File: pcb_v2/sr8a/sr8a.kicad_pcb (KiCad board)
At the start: 2 copper layers, 125.7 x 55.2 mm, 23 parts, among them J2 conn, U1 74LS574, U10 74LS00, U2 74LS574, U3 74LS574, U4 74LS574, U5 74LS574, U6 74LS574, U7 74LS574, U8 74HC238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

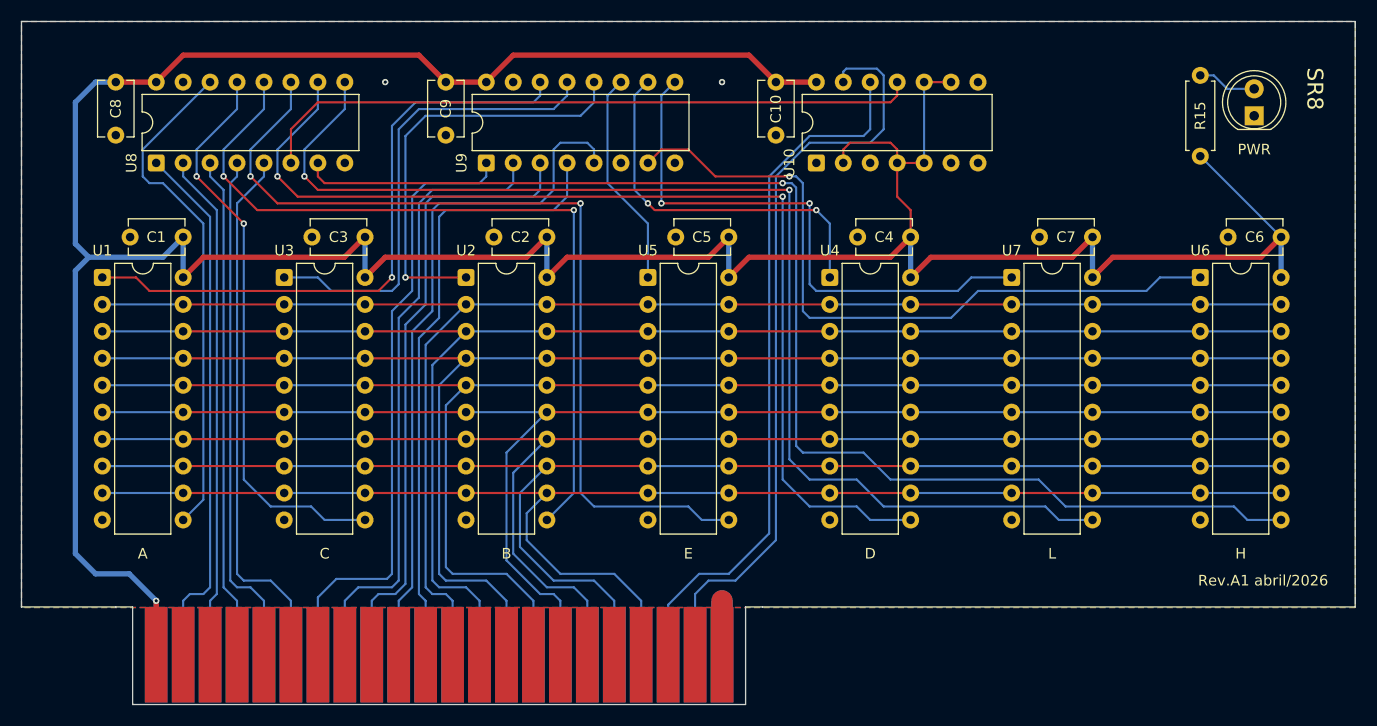
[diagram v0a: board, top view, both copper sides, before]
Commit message: novo layout para ajustar a pinagem do conector
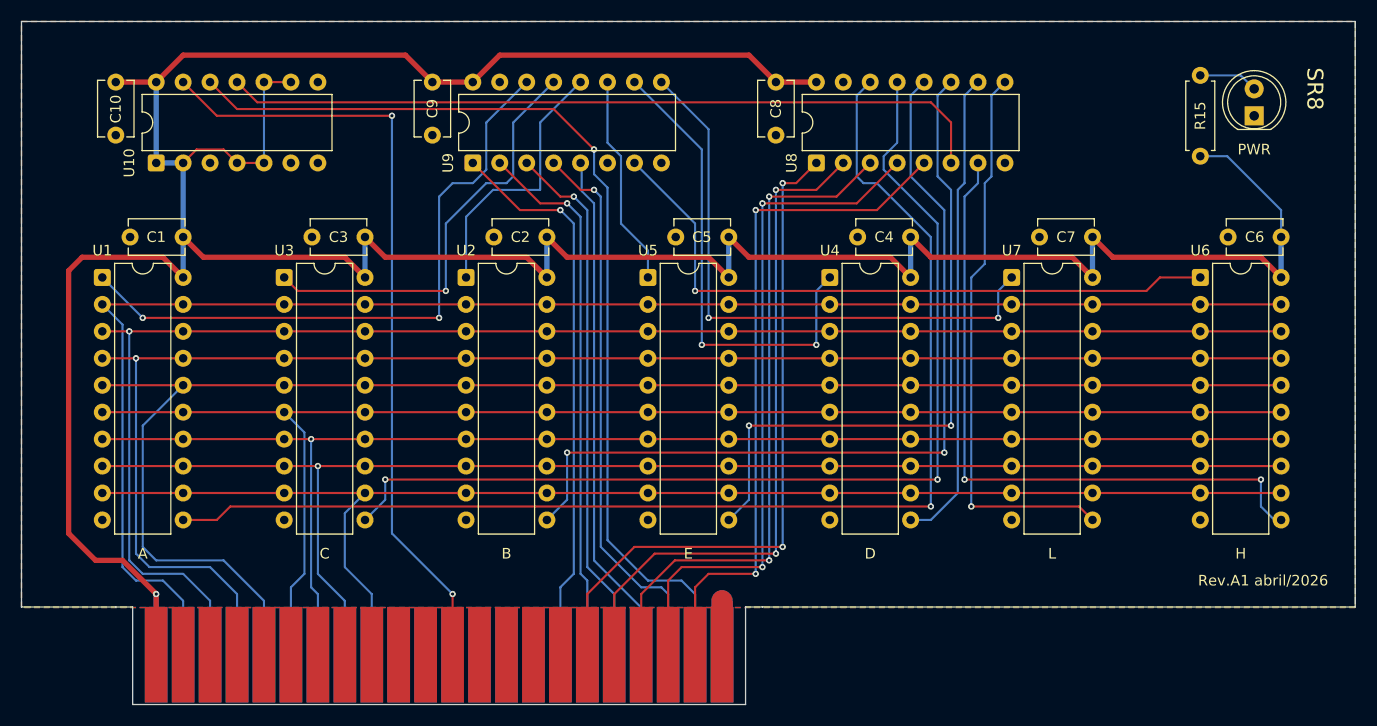
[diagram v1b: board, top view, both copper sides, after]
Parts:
- moved C10 62.2 mm to (54.6, 88.8)
- moved C8 62.2 mm to (116.8, 88.8)
- moved U10 62.2 mm to (58.4, 91.4)
- moved U8 62.2 mm to (120.7, 91.4)
- moved C9 1.27 mm to (84.5, 88.8)
- moved U9 1.27 mm to (88.3, 91.4)
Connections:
- J2 pad 12: unconnected-(J2-Pin_12-Pad12) -> clock
- J2 pad 17: unconnected-(J2-Pin_17-Pad17) -> wr_addr_0
- J2 pad 18: unconnected-(J2-Pin_18-Pad18) -> wr_addr_1
- J2 pad 19: unconnected-(J2-Pin_19-Pad19) -> wr_addr_2
- J2 pad 20: unconnected-(J2-Pin_20-Pad20) -> wr_addr_3
- J2 pad 21: unconnected-(J2-Pin_21-Pad21) -> wr_addr_4
- J2 pad 24: wr_addr_0 -> data_0
- J2 pad 25: wr_addr_1 -> data_1
- J2 pad 26: wr_addr_2 -> data_2
- J2 pad 27: wr_addr_3 -> data_3
- J2 pad 28: wr_addr_4 -> data_4
- J2 pad 29: rd_addr_0 -> data_5
- J2 pad 30: rd_addr_1 -> data_6
- J2 pad 31: rd_addr_2 -> data_7
- J2 pad 32: rd_addr_4 -> unconnected-(J2-Pin_32-Pad32)
- J2 pad 33: rd_addr_3 -> unconnected-(J2-Pin_33-Pad33)
- J2 pad 34: data_0 -> unconnected-(J2-Pin_34-Pad34)
- J2 pad 35: data_1 -> unconnected-(J2-Pin_35-Pad35)
- J2 pad 36: data_2 -> unconnected-(J2-Pin_36-Pad36)
- J2 pad 37: data_3 -> unconnected-(J2-Pin_37-Pad37)
- J2 pad 38: data_4 -> rd_addr_0
- J2 pad 39: data_5 -> rd_addr_1
- J2 pad 40: data_6 -> rd_addr_2
- J2 pad 41: data_7 -> rd_addr_4
- J2 pad 42: wr_enable -> rd_addr_3
- J2 pad 43: clock -> wr_enable
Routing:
- net write_A: track 47.8 -> 115.2 mm, vias 0 -> 1
- net write_L: track 113.1 -> 53.3 mm, vias 2 -> 1
- net write_H: track 119.7 -> 63.3 mm, vias 1 -> 2
- net write_D: track 99.2 -> 45.0 mm, vias 2 -> 0
- net write_C: track 53.9 -> 96.8 mm
- net wr_enable: track 66.5 -> 92.3 mm, vias 0 -> 1
- net write_E: track 85.0 -> 62.2 mm
- net wr_addr_2: track 47.4 -> 64.2 mm, vias 0 -> 2
- net wr_addr_1: track 47.9 -> 64.2 mm, vias 0 -> 2
- net wr_addr_3: track 48.7 -> 65.0 mm, vias 0 -> 2
- net rd_addr_4: track 64.9 -> 48.7 mm
- net ~{read_B}: track 40.1 -> 25.5 mm, vias 1 -> 0
- net wr_addr_0: track 50.3 -> 64.2 mm, vias 0 -> 2
- net wr_addr_4: track 51.0 -> 64.6 mm, vias 0 -> 2
- net write_clock: track 62.9 -> 72.7 mm
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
